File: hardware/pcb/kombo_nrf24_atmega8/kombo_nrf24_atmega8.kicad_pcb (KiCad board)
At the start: 2 copper layers, 37.6 x 30.7 mm, 25 parts, among them J1 Conn_01x02, J2 Conn_01x06, J3 AVR-ISP-6, J4 Conn_01x06, J5 Conn_01x04, J6 Conn_01x04, J7 Conn_01x02, J8 Conn_01x02, J9 Conn_01x02, U1 AMS1117-3.3, U2 ATmega8A-A, U3 NRF24L01_Breakout

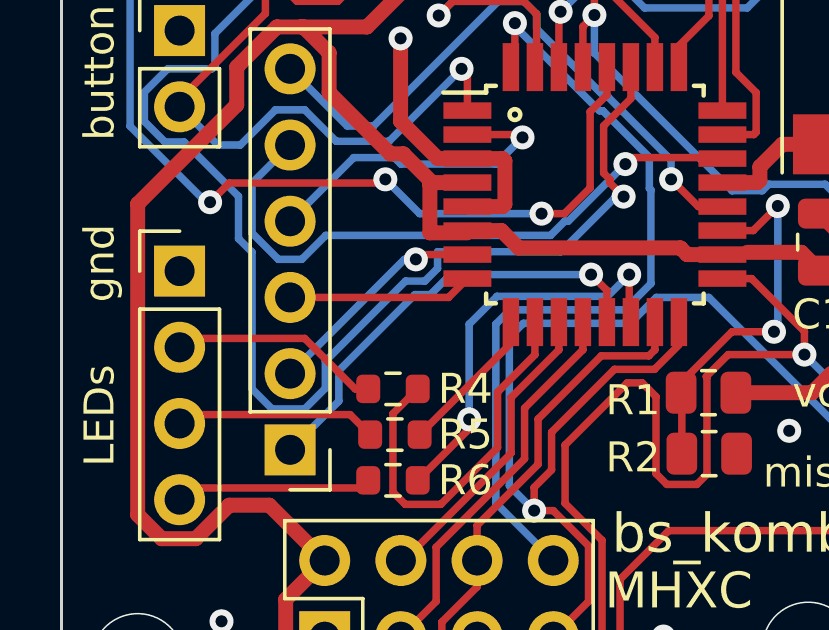
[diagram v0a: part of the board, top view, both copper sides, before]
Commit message: 15/01/2024
✅ - обновлена библиотека работы с модулем nrf24l01+
✅ - добавлена библиотека работы с адресными светодиодами ws2812
✅ - обновлены файлы печатных плат
✅ - добавлены файлы печатных плат микроконтроллера stm32f030f4p6 c nrf24l01+
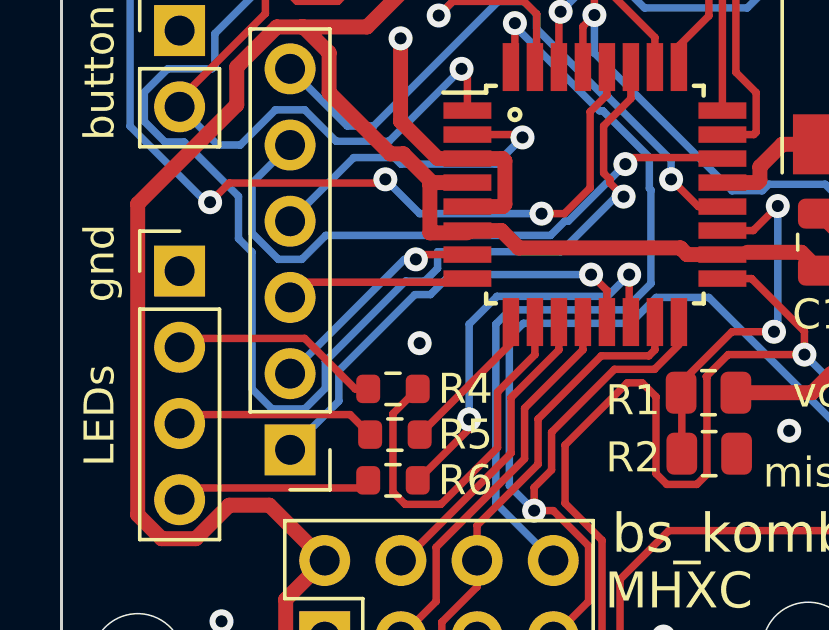
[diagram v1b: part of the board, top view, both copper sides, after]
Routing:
- net GND: vias 9 -> 10
